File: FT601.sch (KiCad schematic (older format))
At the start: 23 parts, among them U1 FT601, U2 ESD7016, U4 ECP5, U5 Si5351, X1 GSB443133HR, Y1 FL3000027, Y2 ABM11-141-26.000MHZ

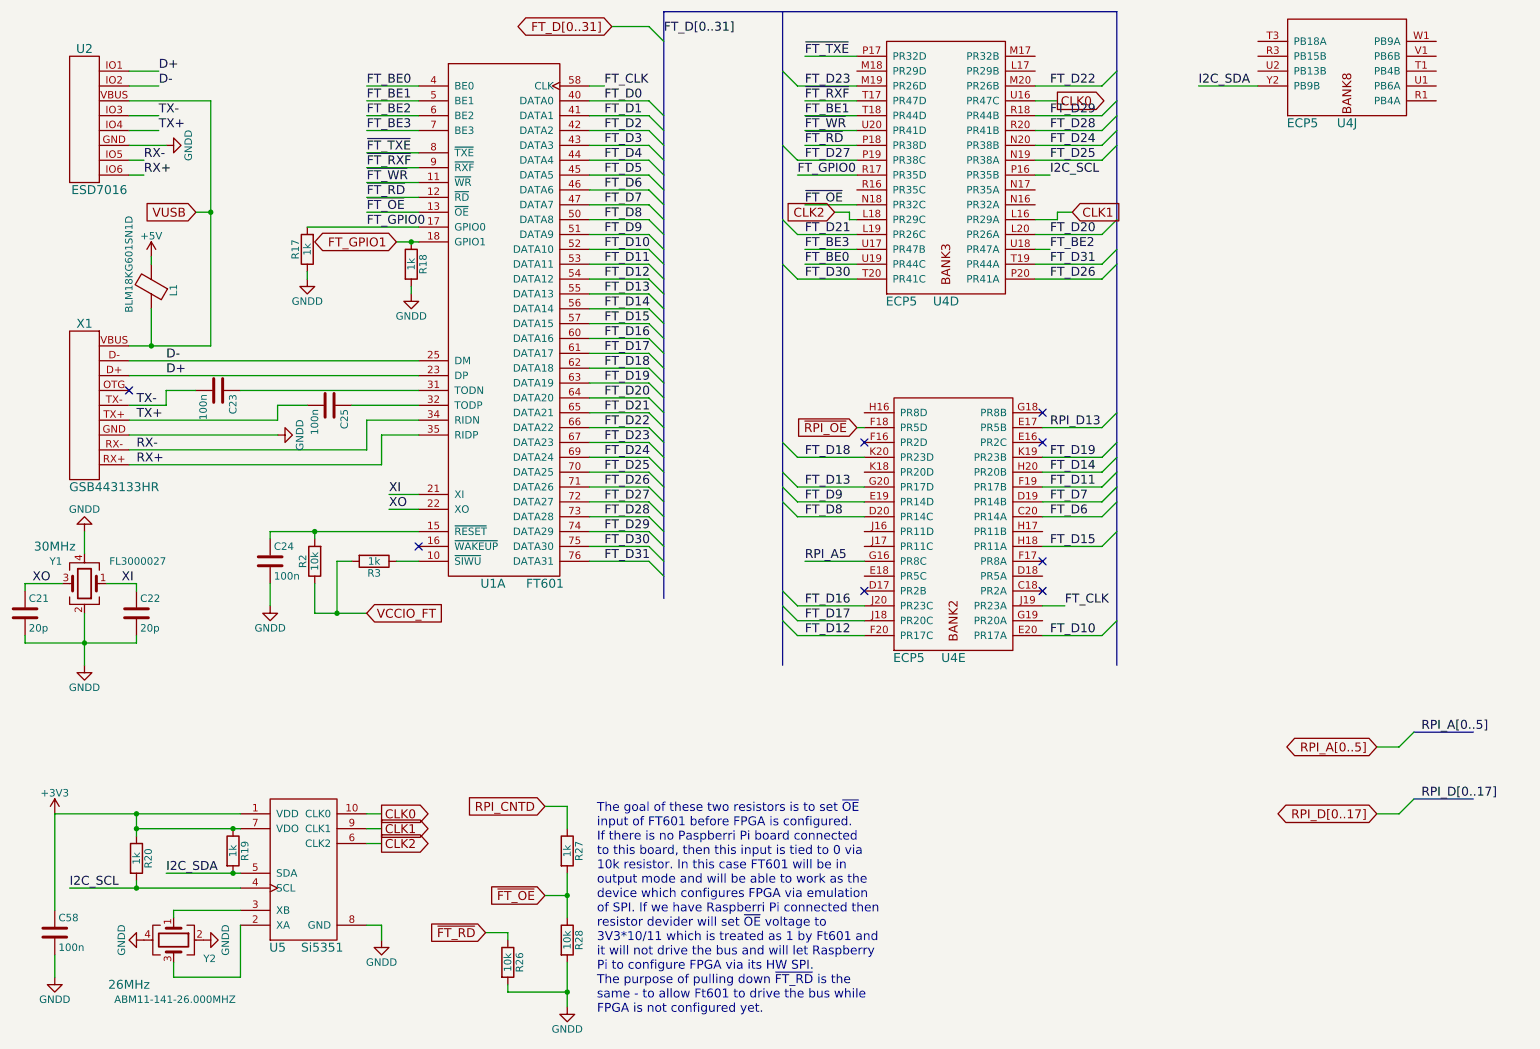
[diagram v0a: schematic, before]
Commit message: Start tracing IO Fix connector for Rpi Use LED indicator for TX/RX LEDs
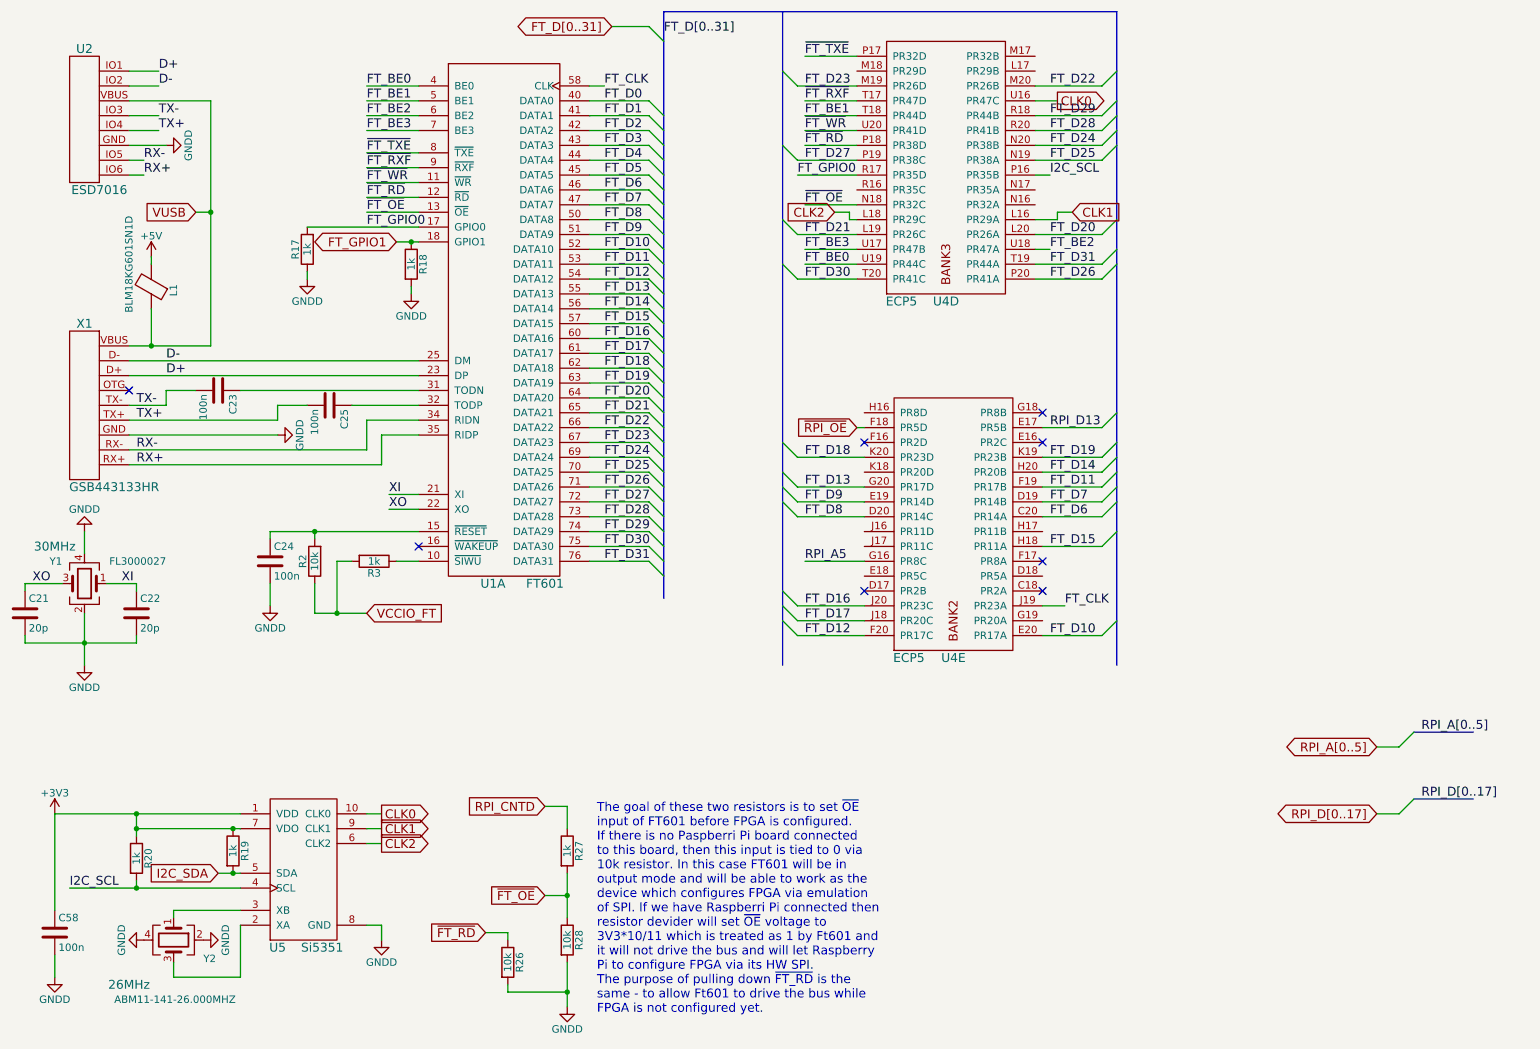
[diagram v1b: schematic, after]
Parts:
- removed unit 10 of U4
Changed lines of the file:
@@
 $EndComp
 $Comp
-L GNDD #PWR062
+L GNDD #PWR066
 U 1 1 58981141
 P 2550 3650
-F 0 "#PWR062" H 2550 3400 50  0001 C CNN
+F 0 "#PWR066" H 2550 3400 50  0001 C CNN
 F 1 "GNDD" H 2550 3500 50  0000 C CNN
 F 2 "" H 2550 3650 50  0000 C CNN
@@
 TX+
 $Comp
-L GNDD #PWR063
+L GNDD #PWR067
 U 1 1 58982448
 P 1800 1700
-F 0 "#PWR063" H 1800 1450 50  0001 C CNN
+F 0 "#PWR067" H 1800 1450 50  0001 C CNN
 F 1 "GNDD" H 1800 1550 50  0000 C CNN
 F 2 "" H 1800 1700 50  0000 C CNN
@@
 $EndComp
 $Comp
-L GNDD #PWR064
+L GNDD #PWR068
 U 1 1 58983172
 P 2500 4800
-F 0 "#PWR064" H 2500 4550 50  0001 C CNN
+F 0 "#PWR068" H 2500 4550 50  0001 C CNN
 F 1 "GNDD" H 2500 4650 50  0000 C CNN
 F 2 "" H 2500 4800 50  0000 C CNN
@@
 $EndComp
 $Comp
-L GNDD #PWR065
+L GNDD #PWR069
 U 1 1 58983AFE
 P 1250 5200
-F 0 "#PWR065" H 1250 4950 50  0001 C CNN
+F 0 "#PWR069" H 1250 4950 50  0001 C CNN
 F 1 "GNDD" H 1250 5050 50  0000 C CNN
 F 2 "" H 1250 5200 50  0000 C CNN
@@
 $EndComp
 $Comp
-L GNDD #PWR066
+L GNDD #PWR070
 U 1 1 58983B6B
 P 1250 4300
-F 0 "#PWR066" H 1250 4050 50  0001 C CNN
+F 0 "#PWR070" H 1250 4050 50  0001 C CNN
 F 1 "GNDD" H 1250 4150 50  0000 C CNN
 F 2 "" H 1250 4300 50  0000 C CNN
@@
 $EndComp
 $Comp
-L GNDD #PWR067
+L GNDD #PWR071
 U 1 1 58A3CED9
 P 3450 2700
-F 0 "#PWR067" H 3450 2450 50  0001 C CNN
+F 0 "#PWR071" H 3450 2450 50  0001 C CNN
 F 1 "GNDD" H 3450 2550 50  0000 C CNN
 F 2 "" H 3450 2700 50  0000 C CNN
@@
 $EndComp
 $Comp
-L GNDD #PWR068
+L GNDD #PWR072
 U 1 1 58A3CF07
 P 2750 2600
-F 0 "#PWR068" H 2750 2350 50  0001 C CNN
+F 0 "#PWR072" H 2750 2350 50  0001 C CNN
 F 1 "GNDD" H 2750 2450 50  0000 C CNN
 F 2 "" H 2750 2600 50  0000 C CNN
@@
 $EndComp
 $Comp
-L +3V3 #PWR069
+L +3V3 #PWR073
 U 1 1 58A3E1D8
 P 1050 6200
-F 0 "#PWR069" H 1050 6050 50  0001 C CNN
+F 0 "#PWR073" H 1050 6050 50  0001 C CNN
 F 1 "+3V3" H 1050 6340 50  0000 C CNN
 F 2 "" H 1050 6200 50  0000 C CNN
@@
 $EndComp
 $Comp
-L GNDD #PWR070
+L GNDD #PWR074
 U 1 1 58A3E3AE
 P 1050 7300
-F 0 "#PWR070" H 1050 7050 50  0001 C CNN
+F 0 "#PWR074" H 1050 7050 50  0001 C CNN
 F 1 "GNDD" H 1050 7150 50  0000 C CNN
 F 2 "" H 1050 7300 50  0000 C CNN
@@
 $EndComp
 $Comp
-L GNDD #PWR071
+L GNDD #PWR075
 U 1 1 58A3F555
 P 2050 7050
-F 0 "#PWR071" H 2050 6800 50  0001 C CNN
+F 0 "#PWR075" H 2050 6800 50  0001 C CNN
 F 1 "GNDD" H 2050 6900 50  0000 C CNN
 F 2 "" H 2050 7050 50  0000 C CNN
@@
 CLK2
 $Comp
-L GNDD #PWR072
+L GNDD #PWR076
 U 1 1 58A415AA
 P 3250 7050
-F 0 "#PWR072" H 3250 6800 50  0001 C CNN
+F 0 "#PWR076" H 3250 6800 50  0001 C CNN
 F 1 "GNDD" H 3250 6900 50  0000 C CNN
 F 2 "" H 3250 7050 50  0000 C CNN
@@
 $EndComp
 $Comp
-L +5V #PWR073
+L +5V #PWR077
 U 1 1 58A3FC7D
 P 1700 2450
-F 0 "#PWR073" H 1700 2300 50  0001 C CNN
+F 0 "#PWR077" H 1700 2300 50  0001 C CNN
 F 1 "+5V" H 1700 2590 50  0000 C CNN
 F 2 "" H 1700 2450 50  0000 C CNN
@@
 	2300 7300 2300 6950
 Wire Wire Line
-	1800 6600 2300 6600
+	2150 6600 2300 6600
 Connection ~ 2250 6600
 Wire Wire Line
@@
 	1050 6200 1050 6850
 $Comp
-L GNDD #PWR074
+L GNDD #PWR078
 U 1 1 58A3F51F
 P 1650 7050
-F 0 "#PWR074" H 1650 6800 50  0001 C CNN
+F 0 "#PWR078" H 1650 6800 50  0001 C CNN
 F 1 "GNDD" H 1650 6900 50  0000 C CNN
 F 2 "" H 1650 7050 50  0000 C CNN
@@
 ~FT_OE
 $Comp
-L GNDD #PWR075
+L GNDD #PWR079
 U 1 1 58ABB46B
 P 4500 7500
-F 0 "#PWR075" H 4500 7250 50  0001 C CNN
+F 0 "#PWR079" H 4500 7250 50  0001 C CNN
 F 1 "GNDD" H 4500 7350 50  0000 C CNN
 F 2 "" H 4500 7500 50  0000 C CNN
@@
 NoConn ~ 7700 3700
 NoConn ~ 7700 4700
-Text Label 1800 6600 0    60   ~ 0
-I2C_SDA
 Text Label 1150 6700 0    60   ~ 0
 I2C_SCL
-Text Label 8750 1300 0    60   ~ 0
-I2C_SDA
 Text Label 7750 1900 0    60   ~ 0
 I2C_SCL
@@
 Wire Wire Line
 	6500 3600 6450 3600
-$Comp
-L ECP5 U4
-U 10 1 58C29E50
-P 9350 1500
-F 0 "U4" H 9750 1450 60  0000 C CNN
-F 1 "ECP5" H 9450 1450 60  0000 C CNN
-F 2 "sdr-foots:ECP5_381" H 7800 2050 60  0001 C CNN
-F 3 "" H 7800 2050 60  0001 C CNN
-	10   9350 1500
-	1    0    0    -1
-$EndComp
-Wire Wire Line
-	9150 1300 8750 1300
 Wire Wire Line
 	7750 1900 7650 1900
@@
 Wire Wire Line
 	6450 1900 6050 1900
+Text GLabel 2150 6600 0    60   Input ~ 0
+I2C_SDA
 $EndSCHEMATC

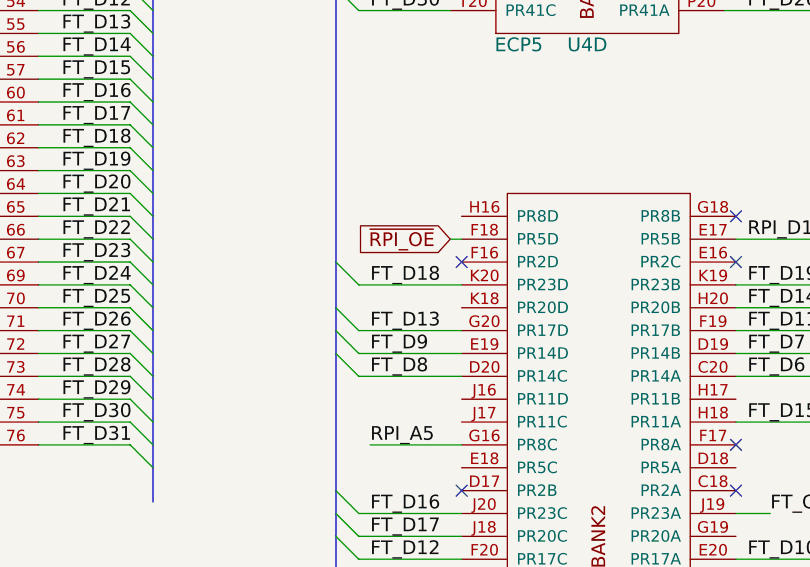
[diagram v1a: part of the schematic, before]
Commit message: Add VCCIO and some vias
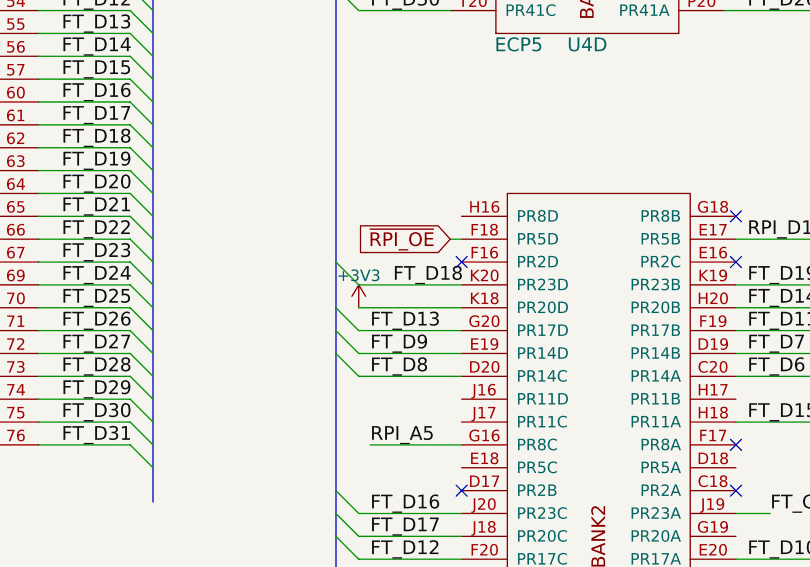
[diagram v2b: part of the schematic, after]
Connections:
- net +3V3: now also U4.K18 (PR20D)

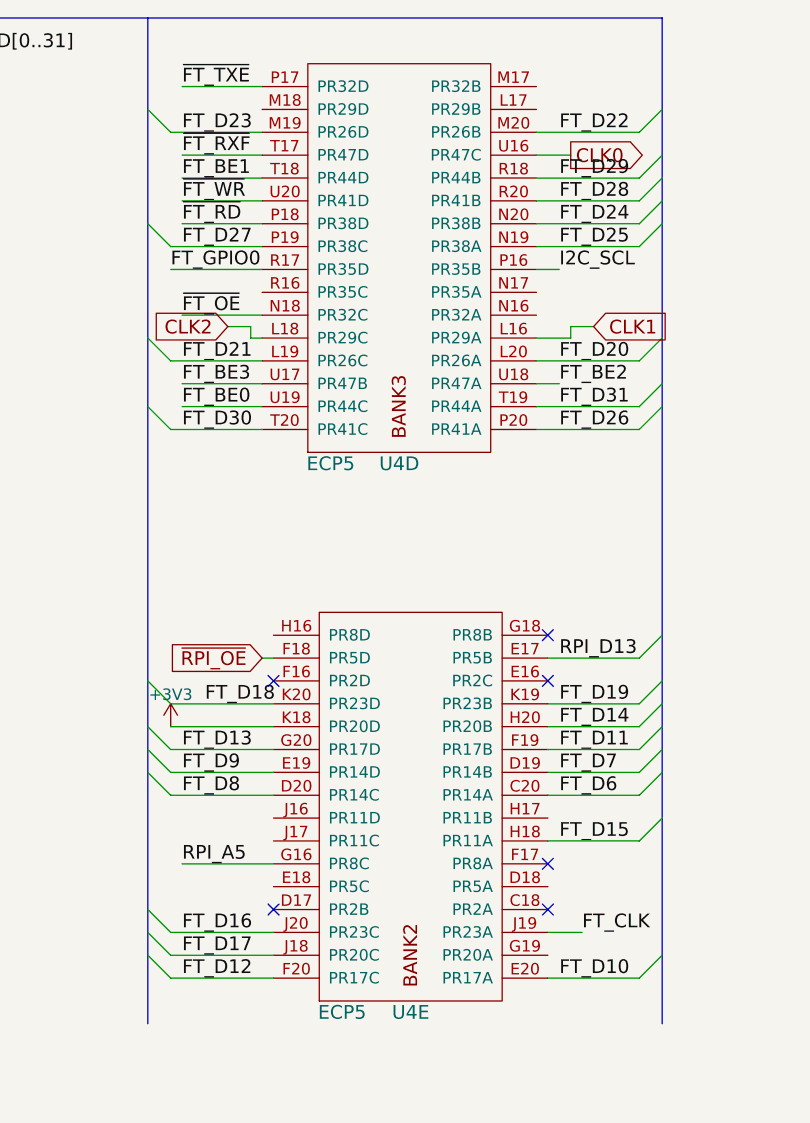
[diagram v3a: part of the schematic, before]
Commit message: FT232H has been finished Not finished: - PROGRAMN button - silkscreen preparation - RF
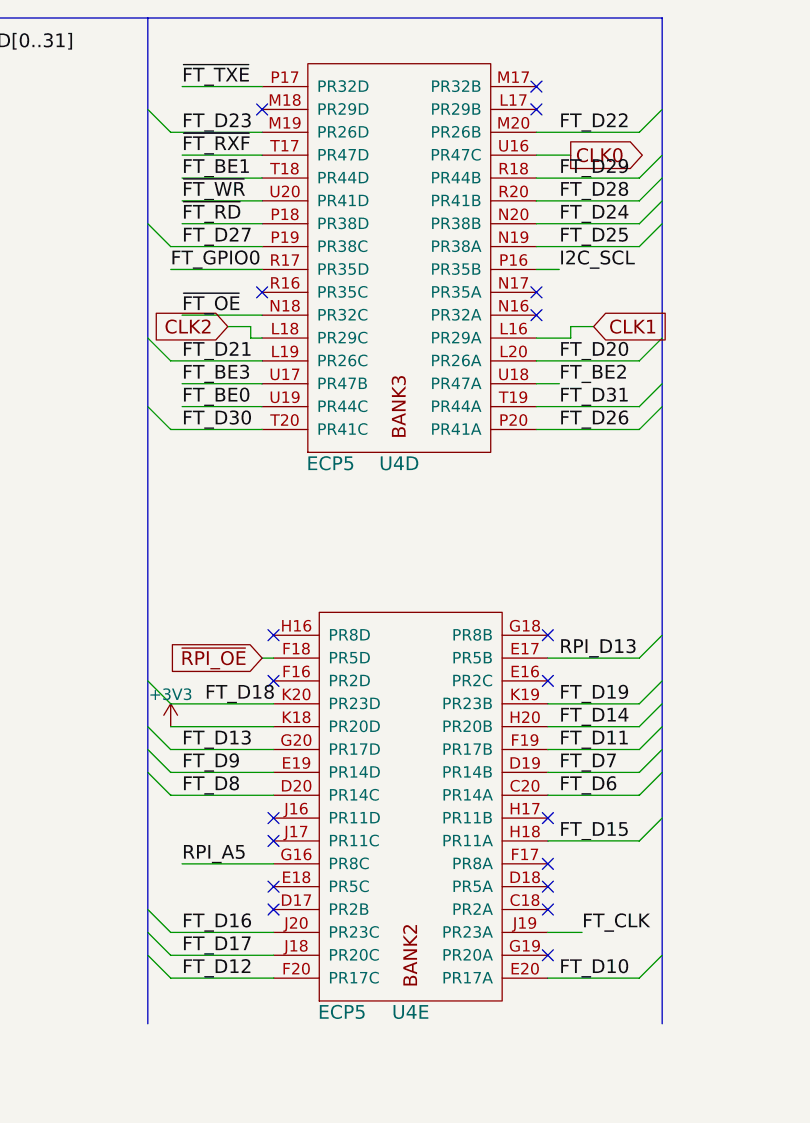
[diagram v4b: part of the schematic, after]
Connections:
- no-connect marks 8 -> 21
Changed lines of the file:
@@
 Wire Wire Line
 	6500 3900 6050 3900
+NoConn ~ 7650 1100
+NoConn ~ 7650 1200
+NoConn ~ 7650 2000
+NoConn ~ 7650 2100
+NoConn ~ 6450 2000
+NoConn ~ 6450 1200
+NoConn ~ 7700 4300
+NoConn ~ 7700 4600
+NoConn ~ 6500 3500
+NoConn ~ 6500 4300
+NoConn ~ 6500 4400
+NoConn ~ 6500 4600
+NoConn ~ 7700 4900
 $EndSCHEMATC
